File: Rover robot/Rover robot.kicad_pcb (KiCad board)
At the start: 2 copper layers, 67 x 54 mm, 13 parts

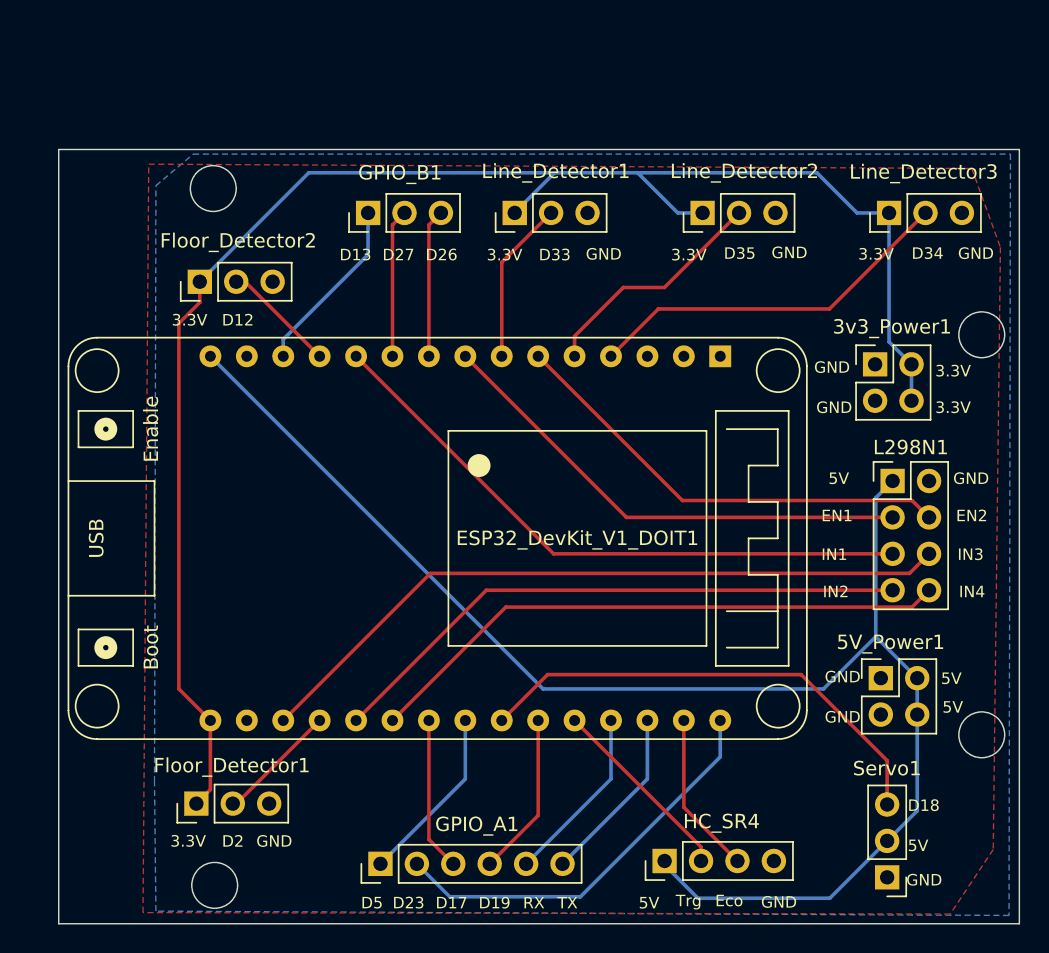
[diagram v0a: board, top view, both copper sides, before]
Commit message: feat: new brick compatible size
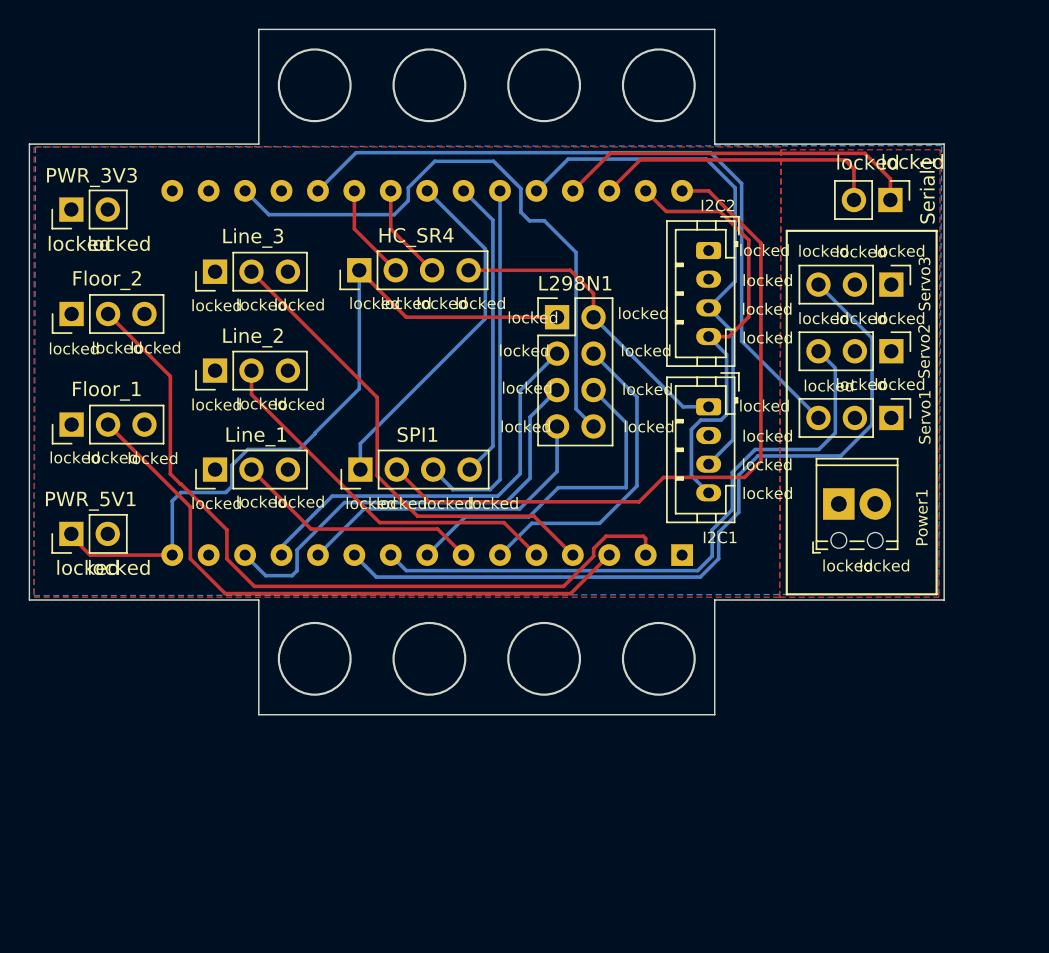
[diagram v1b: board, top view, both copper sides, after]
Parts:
- removed 3v3_Power1, 5V_Power1: Conn_02x02_Odd_Even, Connector_PinHeader_2.54mm:PinHeader_2x02_P2.54mm_Vertical
- removed GPIO_A1: Conn_01x06_Pin, Connector_PinHeader_2.54mm:PinHeader_1x06_P2.54mm_Vertical
- removed GPIO_B1: Conn_01x03_Pin, Connector_PinHeader_2.54mm:PinHeader_1x03_P2.54mm_Vertical
- added I2C1: I2C, Connector_JST:JST_PH_B4B-PH-K_1x04_P2.00mm_Vertical, F.Cu at (147.4, 118.3)
- added I2C2: I2C, Connector_JST:JST_PH_B4B-PH-K_1x04_P2.00mm_Vertical, F.Cu at (147.4, 107.4)
- added PWR_3V3: Conn_3V3, Connector_PinHeader_2.54mm:PinHeader_1x02_P2.54mm_Vertical, F.Cu at (103.0, 104.6)
- added PWR_5V1: Conn_5V, Connector_PinHeader_2.54mm:PinHeader_1x02_P2.54mm_Vertical, F.Cu at (103.0, 127.2)
- added Power1: Screw_Terminal_01x02, TerminalBlock_Phoenix:TerminalBlock_Phoenix_MPT-0,5-2-2.54_1x02_P2.54mm_Horizontal, F.Cu at (156.5, 125.1)
- added SPI1: Conn_01x04_Pin, Connector_PinHeader_2.54mm:PinHeader_1x04_P2.54mm_Vertical, F.Cu at (123.2, 122.7)
- added Serial1: Serial, Connector_PinHeader_2.54mm:PinHeader_1x02_P2.54mm_Vertical, F.Cu at (160.1, 103.9)
- added Servo2: Conn_01x03_Pin, Connector_PinHeader_2.54mm:PinHeader_1x03_P2.54mm_Vertical, F.Cu at (160.2, 114.5)
- added Servo3: Conn_01x03_Pin, Connector_PinHeader_2.54mm:PinHeader_1x03_P2.54mm_Vertical, F.Cu at (160.2, 109.8)
- ESP32_DevKit_V1_DOIT1: footprint ESP32_DevKit_V1_DOIT:esp32_devkit_v1_doit -> ESP32_DevKit_V1_DOIT:esp32_devkit_v1_doit_simplified; moved to B.Cu
- moved Line_3 47.2 mm to (113.0, 108.9)
- moved HC_SR4 46.4 mm to (123.1, 108.8)
- moved Line_2 35.7 mm to (113.0, 115.8)
- moved Servo1 32.0 mm to (160.2, 119.1), turned to -90 degrees
- moved Floor_1 27.8 mm to (103.0, 119.6)
- moved Line_1 27.5 mm to (113.0, 122.7)
- moved L298N1 26.0 mm to (136.9, 112.1)
- moved ESP32_DevKit_V1_DOIT1 11.8 mm to (145.6, 116.0), turned to 90 degrees
- moved Floor_2 9.22 mm to (103.0, 111.8)
- renumbered Floor_Detector1 to Floor_1, Floor_Detector2 to Floor_2, Line_Detector1 to Line_1, Line_Detector2 to Line_2, Line_Detector3 to Line_3
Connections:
- ESP32_DevKit_V1_DOIT1 pad 19: Net-(ESP32_DevKit_V1_DOIT1-IO2) -> unconnected-(ESP32_DevKit_V1_DOIT1-IO2-Pad19)
- ESP32_DevKit_V1_DOIT1 pad 2: unconnected-(ESP32_DevKit_V1_DOIT1-SENSOR_VP-Pad2) -> Net-(ESP32_DevKit_V1_DOIT1-SENSOR_VP)
- ESP32_DevKit_V1_DOIT1 pad 23: Net-(ESP32_DevKit_V1_DOIT1-IO5) -> VCS
- ESP32_DevKit_V1_DOIT1 pad 24: Net-(ESP32_DevKit_V1_DOIT1-IO18) -> VCLK
- ESP32_DevKit_V1_DOIT1 pad 25: Net-(ESP32_DevKit_V1_DOIT1-IO19) -> VMISO
- ESP32_DevKit_V1_DOIT1 pad 26: Net-(ESP32_DevKit_V1_DOIT1-IO21) -> SDA
- ESP32_DevKit_V1_DOIT1 pad 29: Net-(ESP32_DevKit_V1_DOIT1-IO22) -> SCL
- ESP32_DevKit_V1_DOIT1 pad 3: unconnected-(ESP32_DevKit_V1_DOIT1-SENSOR_VN-Pad3) -> Net-(ESP32_DevKit_V1_DOIT1-SENSOR_VN)
- ESP32_DevKit_V1_DOIT1 pad 30: Net-(ESP32_DevKit_V1_DOIT1-IO23) -> VMOSI
- Floor_1 pad 2: Net-(ESP32_DevKit_V1_DOIT1-IO2) -> Net-(ESP32_DevKit_V1_DOIT1-SENSOR_VN)
- Floor_2 pad 2: Net-(ESP32_DevKit_V1_DOIT1-IO12) -> Net-(ESP32_DevKit_V1_DOIT1-SENSOR_VP)
- HC_SR4 pad 2: Net-(ESP32_DevKit_V1_DOIT1-IO21) -> Net-(ESP32_DevKit_V1_DOIT1-IO16)
- HC_SR4 pad 3: Net-(ESP32_DevKit_V1_DOIT1-IO22) -> Net-(ESP32_DevKit_V1_DOIT1-IO17)
- L298N1 pad 3: Net-(ESP32_DevKit_V1_DOIT1-IO25) -> Net-(ESP32_DevKit_V1_DOIT1-IO12)
- L298N1 pad 5: Net-(ESP32_DevKit_V1_DOIT1-IO14) -> Net-(ESP32_DevKit_V1_DOIT1-IO13)
- L298N1 pad 6: Net-(ESP32_DevKit_V1_DOIT1-IO15) -> Net-(ESP32_DevKit_V1_DOIT1-IO25)
- L298N1 pad 7: Net-(ESP32_DevKit_V1_DOIT1-IO4) -> Net-(ESP32_DevKit_V1_DOIT1-IO14)
- L298N1 pad 8: Net-(ESP32_DevKit_V1_DOIT1-IO16) -> Net-(ESP32_DevKit_V1_DOIT1-IO15)
- Servo1 pad 2: +5V -> +9V
- Servo1 pad 3: Net-(ESP32_DevKit_V1_DOIT1-IO18) -> Net-(ESP32_DevKit_V1_DOIT1-IO4)
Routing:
- net +3.3V: track 114.1 -> 0.00 mm
- net Net-(ESP32_DevKit_V1_DOIT1-SENSOR_VP): track 0.00 -> 53.5 mm
- net +5V: track 103.6 -> 52.1 mm
- net VMOSI: track 0.00 -> 49.7 mm
- net Net-(ESP32_DevKit_V1_DOIT1-IO27): track 10.3 -> 55.1 mm
- net Net-(ESP32_DevKit_V1_DOIT1-SENSOR_VN): track 0.00 -> 43.1 mm
- net SDA: track 0.00 -> 37.1 mm
- net Net-(ESP32_DevKit_V1_DOIT1-IO16): track 41.2 -> 6.73 mm
- net Net-(ESP32_DevKit_V1_DOIT1-IO26): track 10.3 -> 44.2 mm
- net Net-(ESP32_DevKit_V1_DOIT1-IO18): track 33.8 -> 0.00 mm
- net SCL: track 0.00 -> 31.1 mm
- net Net-(ESP32_DevKit_V1_DOIT1-IO23): track 28.7 -> 0.00 mm
- net VMISO: track 0.00 -> 25.7 mm
- net VCS: track 0.00 -> 24.7 mm
- net GND: track 0.41 -> 21.7 mm
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- added copper zone on F.Cu, net +3.3V
- added copper zone on F.Cu, net +9V
- removed copper zone on F.Cu, net GND
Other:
- board size 67 x 54 mm -> 63.8 x 47.8 mm
- board text added: "locked"
- board text removed: "3.3V"
- board text removed: "5V"
- board text removed: "D12"
- board text removed: "D13"
- board text removed: "D17"
- board text removed: "D18"
- board text removed: "D19"
- board text removed: "D2"
- board text removed: "D23"
- board text removed: "D26"
- board text removed: "D27"
- board text removed: "D33"
- board text removed: "D34"
- board text removed: "D35"
- board text removed: "D5"
- board text removed: "EN1"
- board text removed: "EN2"
- board text removed: "Eco"
- board text removed: "GND"
- board text removed: "IN1"
- board text removed: "IN2"
- board text removed: "IN3"
- board text removed: "IN4"
- board text removed: "RX"
- board text removed: "Rover Robot Board for ESP32 DevKit 1.0 Doit"
- board text removed: "TX"
- board text removed: "Trg"

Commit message: Produced version of the first brick variant
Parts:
- added KiCad: KiCad-Logo2_5mm_SilkScreen, Symbol:KiCad-Logo2_5mm_SilkScreen, B.Cu at (128.0, 112.8)
- added REF**: OSHW-Logo2_7.3x6mm_SilkScreen, Symbol:OSHW-Logo2_7.3x6mm_SilkScreen, B.Cu at (128.0, 118.9)
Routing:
- net +5V: track 52.1 -> 53.1 mm
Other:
- board text added: "https://github.com/deuteros76/rover-robot-PCB"
- board text removed: "Designed by Deuteros https://github.com/deuteros76"

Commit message: refactor: minor changes
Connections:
- ESP32_DevKit_V1_DOIT1 pad 14: GND -> unconnected-(ESP32_DevKit_V1_DOIT1-GND-Pad14)
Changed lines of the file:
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@@
   (net 29 "VMOSI")
   (net 30 "+9V")
+  (net 31 "unconnected-(ESP32_DevKit_V1_DOIT1-GND-Pad14)")
   (footprint "Connector_PinHeader_2.54mm:PinHeader_1x03_P2.54mm_Vertical" locked (layer "F.Cu")
     (at 113.025 115.8 90)
@@
       (net 18 "Net-(ESP32_DevKit_V1_DOIT1-IO13)") (pinfunction "IO13") (pintype "bidirectional"))
     (pad "14" thru_hole circle locked (at -12.7 -33.02 90) (size 1.524 1.524) (drill 0.762) (layers "*.Cu" "*.Mask")
-      (net 2 "GND") (pinfunction "GND") (pintype "power_in"))
+      (net 31 "unconnected-(ESP32_DevKit_V1_DOIT1-GND-Pad14)") (pinfunction "GND") (pintype "power_in"))
     (pad "15" thru_hole circle locked (at -12.7 -35.56 90) (size 1.524 1.524) (drill 0.762) (layers "*.Cu" "*.Mask")
       (net 3 "+5V") (pinfunction "VIN") (pintype "power_in"))
